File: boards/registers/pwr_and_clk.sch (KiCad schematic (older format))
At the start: 23 parts

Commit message: Fix unconnected nets
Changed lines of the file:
@@
 	1    0    0    -1
 $EndComp
+$Comp
+L power:PWR_FLAG #FLG?
+U 1 1 5EF82079
+P 9650 1200
+F 0 "#FLG?" H 9650 1275 50  0001 C CNN
+F 1 "PWR_FLAG" H 9650 1373 50  0000 C CNN
+F 2 "" H 9650 1200 50  0001 C CNN
+F 3 "~" H 9650 1200 50  0001 C CNN
+	1    9650 1200
+	1    0    0    -1
+$EndComp
+$Comp
+L power:GND #PWR?
+U 1 1 5EF830E9
+P 9650 1200
+F 0 "#PWR?" H 9650 950 50  0001 C CNN
+F 1 "GND" H 9655 1027 50  0000 C CNN
+F 2 "" H 9650 1200 50  0001 C CNN
+F 3 "" H 9650 1200 50  0001 C CNN
+	1    9650 1200
+	1    0    0    -1
+$EndComp
+$Comp
+L power:VCC #PWR?
+U 1 1 5EF8368B
+P 10050 1200
+F 0 "#PWR?" H 10050 1050 50  0001 C CNN
+F 1 "VCC" H 10067 1373 50  0000 C CNN
+F 2 "" H 10050 1200 50  0001 C CNN
+F 3 "" H 10050 1200 50  0001 C CNN
+	1    10050 1200
+	1    0    0    -1
+$EndComp
+$Comp
+L power:PWR_FLAG #FLG?
+U 1 1 5EF840F1
+P 10050 1200
+F 0 "#FLG?" H 10050 1275 50  0001 C CNN
+F 1 "PWR_FLAG" H 10050 1373 50  0000 C CNN
+F 2 "" H 10050 1200 50  0001 C CNN
+F 3 "~" H 10050 1200 50  0001 C CNN
+	1    10050 1200
+	-1   0    0    1
+$EndComp
 $EndSCHEMATC

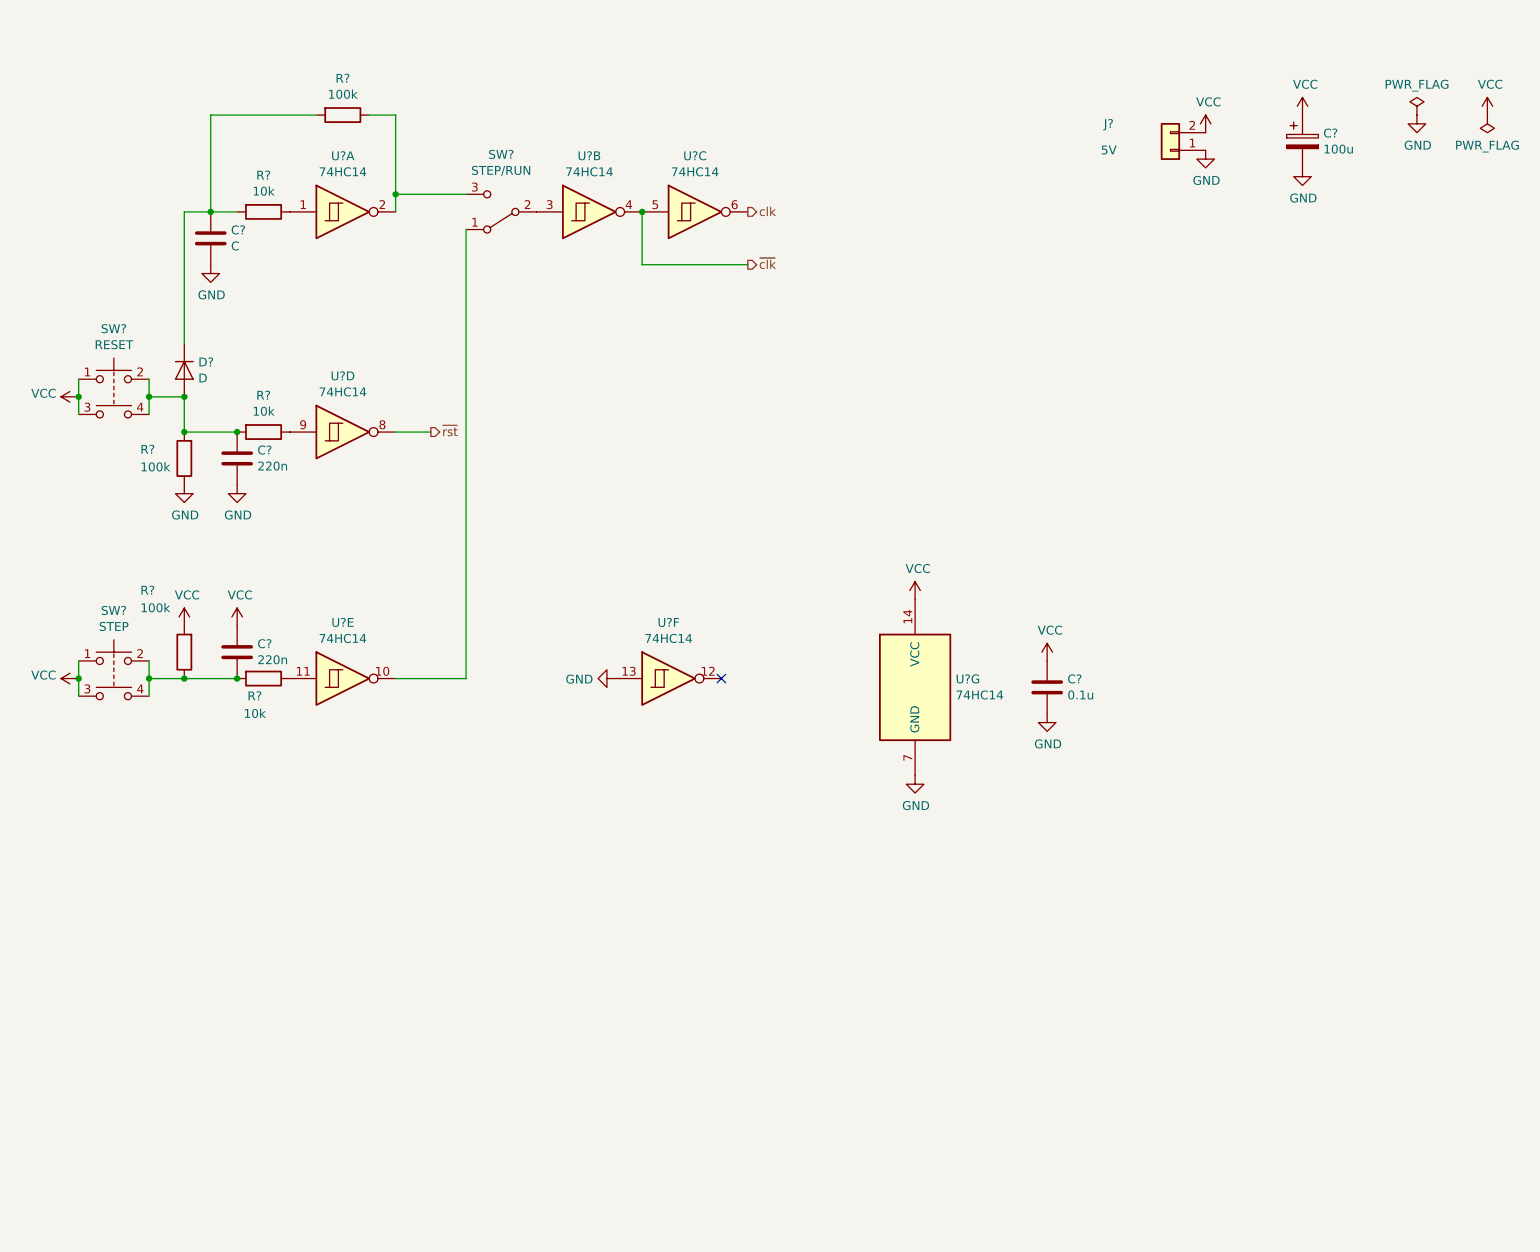
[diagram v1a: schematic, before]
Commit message: Annotated schematics, assigned footprints
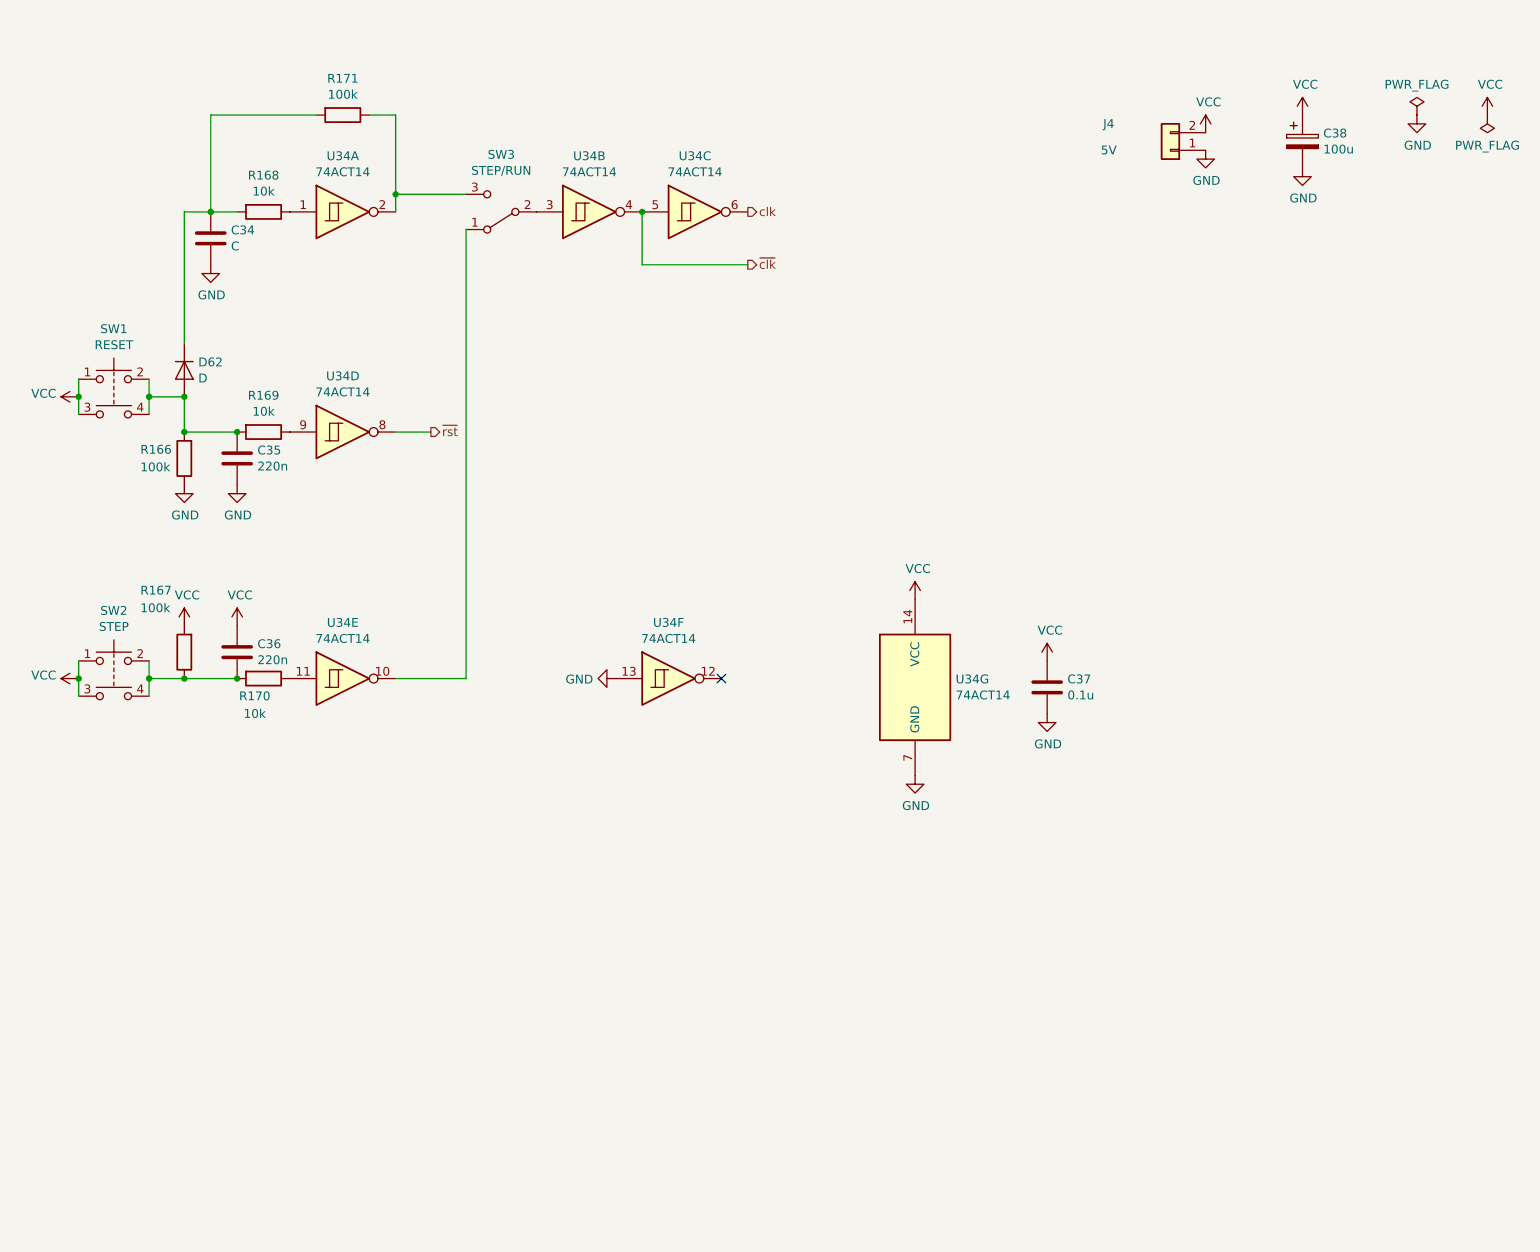
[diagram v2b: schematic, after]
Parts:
- C34, C35, C36: renamed from C?; footprint (none) -> Capacitor_SMD:C_0805_2012Metric
- C37, C38: renamed from C?; footprint (none) -> LED_SMD:LED_0805_2012Metric
- D62: renamed from D?; footprint (none) -> Diode_SMD:D_MiniMELF
- J4: renamed from J?; footprint (none) -> Connector_PinHeader_2.54mm:PinHeader_1x02_P2.54mm_Vertical
- R166, R167, R168, R169, R170, R171: renamed from R?; footprint (none) -> Resistor_SMD:R_0805_2012Metric
- SW1, SW2: renamed from SW?; footprint (none) -> Button_Switch_THT:SW_TH_Tactile_Omron_B3F-10xx
- SW3: renamed from SW?; footprint (none) -> Button_Switch_THT:SW_Slide_1P2T_CK_OS102011MS2Q
- U34: renamed from U?; value 74HC14 -> 74ACT14; footprint (none) -> Package_SO:TSSOP-14_4.4x5mm_P0.65mm

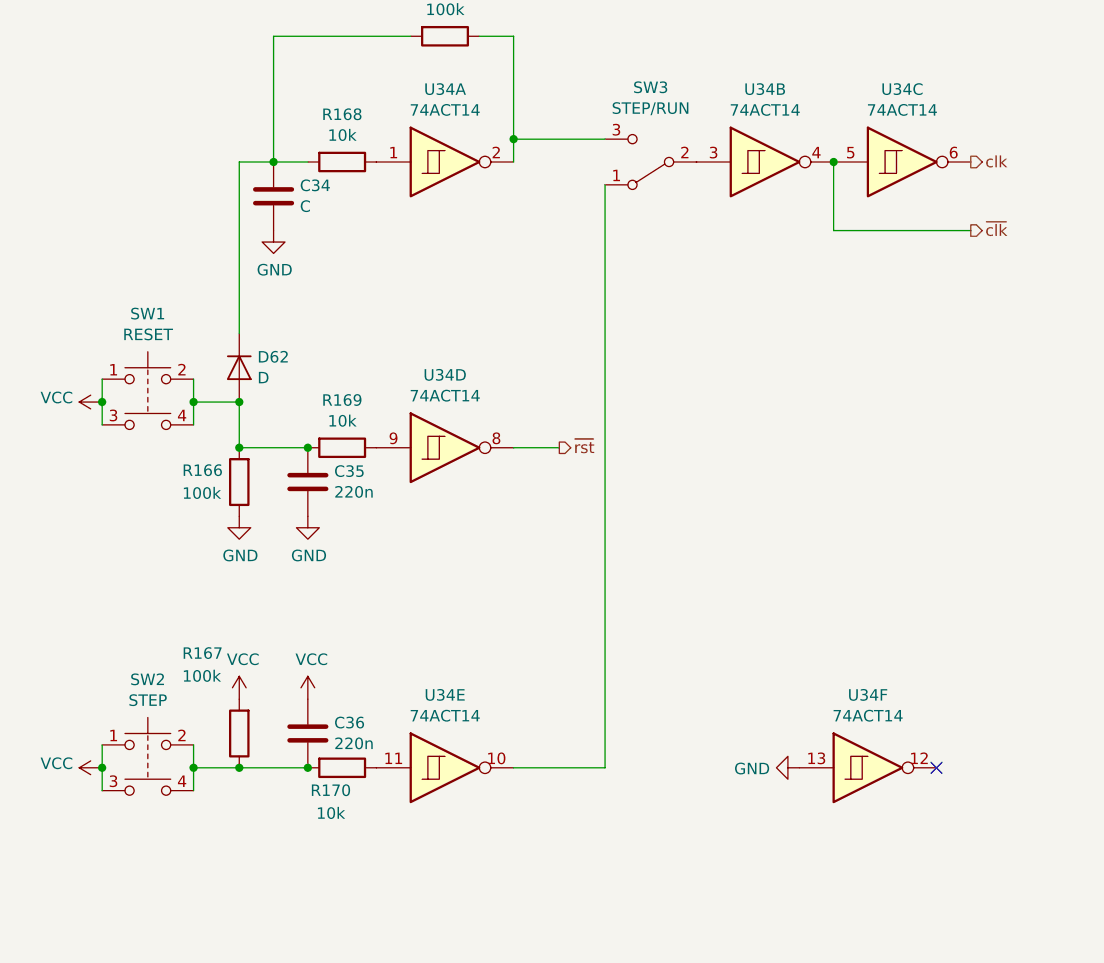
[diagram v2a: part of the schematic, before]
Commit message: CPU registers board
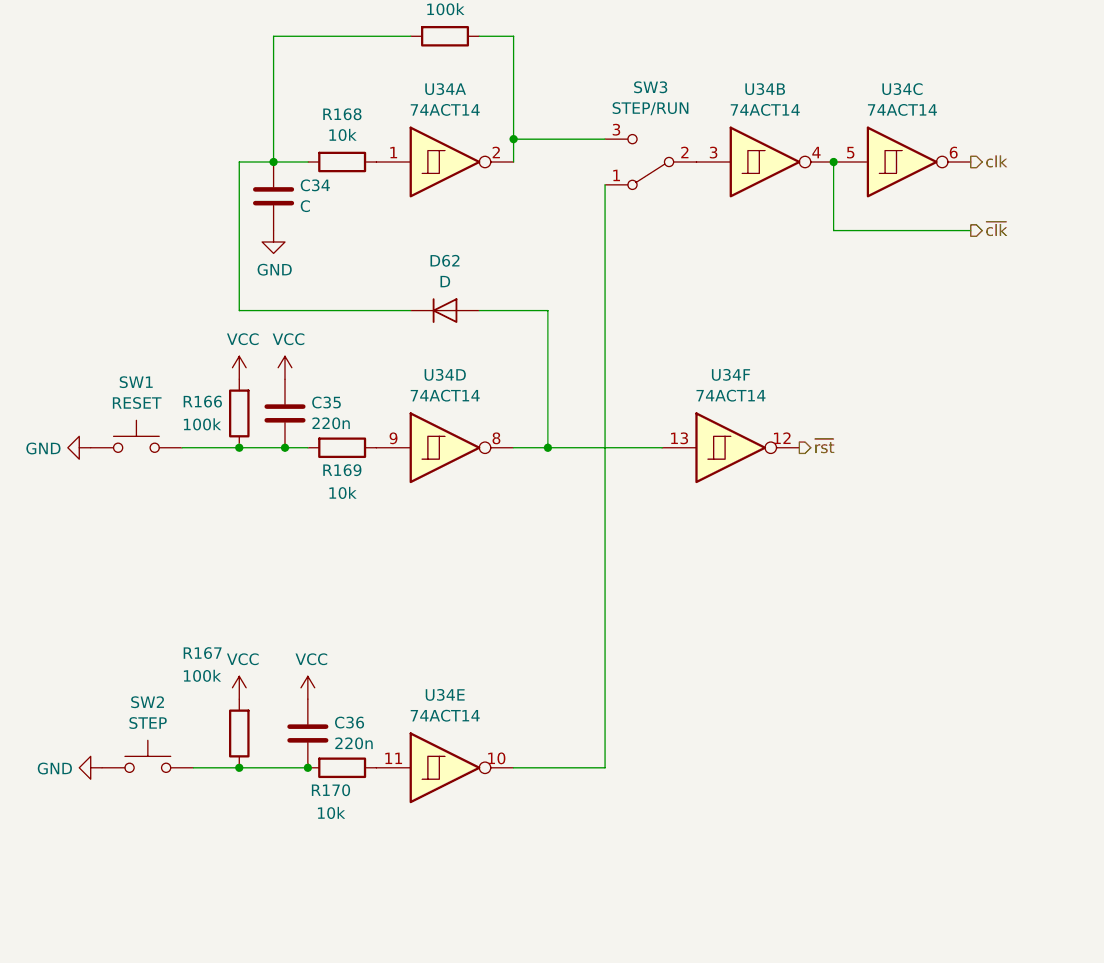
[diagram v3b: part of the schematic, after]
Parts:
- removed SW1: RESET, Button_Switch_THT:SW_TH_Tactile_Omron_B3F-10xx, symbol Switch:SW_Push_Dual
- removed SW2: STEP, Button_Switch_THT:SW_TH_Tactile_Omron_B3F-10xx, symbol Switch:SW_Push_Dual
- added SW1: RESET, Button_Switch_THT:SW_PUSH_6mm, symbol Switch:SW_Push
- added SW2: STEP, Button_Switch_THT:SW_PUSH_6mm, symbol Switch:SW_Push
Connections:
- net GND: now also SW1.1, SW2.1; no longer C35.2, R166.1, U34.13
- net VCC: now also C35.1, R166.2
- net ~rst: now also U34.12; no longer U34.8
- net at C36.2, R167.1, R170.2: now also SW2.2
- new net: C35.2, R166.1, R169.2, SW1.2
- new net: D62.2 (A), U34.13, U34.8
- no-connect marks 1 -> 0
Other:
- moved on the sheet: C35, D62, R166, U34F
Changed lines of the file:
@@
 Text HLabel 5850 1750 2    50   Output ~ 0
 clk
-Text HLabel 4050 3000 2    50   Output ~ 0
+Text HLabel 5100 3000 2    50   Output ~ 0
 ~rst
 Text HLabel 5850 2050 2    50   Output ~ 0
@@
 L Device:R R166
 U 1 1 5EF0FCD1
-P 2650 3150
-F 0 "R166" H 2900 3100 50  0000 R CNN
-F 1 "100k" H 2900 3200 50  0000 R CNN
-F 2 "Resistor_SMD:R_0805_2012Metric" V 2580 3150 50  0001 C CNN
-F 3 "~" H 2650 3150 50  0001 C CNN
-	1    2650 3150
+P 2650 2850
+F 0 "R166" H 2900 2800 50  0000 R CNN
+F 1 "100k" H 2900 2900 50  0000 R CNN
+F 2 "Resistor_SMD:R_0805_2012Metric" V 2580 2850 50  0001 C CNN
+F 3 "~" H 2650 2850 50  0001 C CNN
+	1    2650 2850
 	-1   0    0    1
-$EndComp
-$Comp
-L power:GND #PWR0219
-U 1 1 5EF10373
-P 2650 3300
-F 0 "#PWR0219" H 2650 3050 50  0001 C CNN
-F 1 "GND" H 2655 3127 50  0000 C CNN
-F 2 "" H 2650 3300 50  0001 C CNN
-F 3 "" H 2650 3300 50  0001 C CNN
-	1    2650 3300
-	1    0    0    -1
 $EndComp
 $Comp
@@
 U 1 1 5EF12F5C
 P 3100 3000
-F 0 "R169" V 2893 3000 50  0000 C CNN
-F 1 "10k" V 2984 3000 50  0000 C CNN
+F 0 "R169" V 3200 3000 50  0000 C CNN
+F 1 "10k" V 3300 3000 50  0000 C CNN
 F 2 "Resistor_SMD:R_0805_2012Metric" V 3030 3000 50  0001 C CNN
 F 3 "~" H 3100 3000 50  0001 C CNN
@@
 L Device:C C35
 U 1 1 5EF136E4
-P 2950 3150
-F 0 "C35" H 3065 3196 50  0000 L CNN
-F 1 "220n" H 3065 3105 50  0000 L CNN
-F 2 "Capacitor_SMD:C_0805_2012Metric" H 2988 3000 50  0001 C CNN
-F 3 "~" H 2950 3150 50  0001 C CNN
-	1    2950 3150
-	1    0    0    -1
-$EndComp
-$Comp
-L power:GND #PWR0222
-U 1 1 5EF14A7A
-P 2950 3300
-F 0 "#PWR0222" H 2950 3050 50  0001 C CNN
-F 1 "GND" H 2955 3127 50  0000 C CNN
-F 2 "" H 2950 3300 50  0001 C CNN
-F 3 "" H 2950 3300 50  0001 C CNN
-	1    2950 3300
-	1    0    0    -1
-$EndComp
-Wire Wire Line
-	2650 3000 2950 3000
-Connection ~ 2950 3000
-$Comp
-L Switch:SW_Push_Dual SW1
-U 1 1 5EF16B54
-P 2250 2700
-F 0 "SW1" H 2250 2985 50  0000 C CNN
-F 1 "RESET" H 2250 2894 50  0000 C CNN
-F 2 "Button_Switch_THT:SW_TH_Tactile_Omron_B3F-10xx" H 2250 2900 50  0001 C CNN
-F 3 "~" H 2250 2900 50  0001 C CNN
-	1    2250 2700
-	1    0    0    -1
-$EndComp
-Wire Wire Line
-	2450 2700 2450 2800
-Wire Wire Line
-	2650 3000 2650 2800
-Wire Wire Line
-	2650 2800 2450 2800
-Connection ~ 2650 3000
-Connection ~ 2450 2800
-Wire Wire Line
-	2450 2800 2450 2900
-Wire Wire Line
-	2050 2700 2050 2800
-$Comp
-L power:VCC #PWR0217
-U 1 1 5EF17FE7
-P 2050 2800
-F 0 "#PWR0217" H 2050 2650 50  0001 C CNN
-F 1 "VCC" V 2068 2927 50  0000 L CNN
-F 2 "" H 2050 2800 50  0001 C CNN
-F 3 "" H 2050 2800 50  0001 C CNN
-	1    2050 2800
-	0    -1   -1   0
-$EndComp
-Connection ~ 2050 2800
-Wire Wire Line
-	2050 2800 2050 2900
+P 2850 2850
+F 0 "C35" H 2965 2896 50  0000 L CNN
+F 1 "220n" H 2965 2805 50  0000 L CNN
+F 2 "Capacitor_SMD:C_0805_2012Metric" H 2888 2700 50  0001 C CNN
+F 3 "~" H 2850 2850 50  0001 C CNN
+	1    2850 2850
+	1    0    0    -1
+$EndComp
+Wire Wire Line
+	2650 3000 2850 3000
 $Comp
 L Device:D D62
 U 1 1 5EF19BA6
-P 2650 2650
-F 0 "D62" V 2604 2729 50  0000 L CNN
-F 1 "D" V 2695 2729 50  0000 L CNN
-F 2 "Diode_SMD:D_MiniMELF" H 2650 2650 50  0001 C CNN
-F 3 "~" H 2650 2650 50  0001 C CNN
-	1    2650 2650
-	0    1    1    0
-$EndComp
-Connection ~ 2650 2800
-Wire Wire Line
-	2650 2500 2650 1750
+P 3550 2400
+F 0 "D62" H 3550 2616 50  0000 C CNN
+F 1 "D" H 3550 2525 50  0000 C CNN
+F 2 "Diode_SMD:D_MiniMELF" H 3550 2400 50  0001 C CNN
+F 3 "~" H 3550 2400 50  0001 C CNN
+	1    3550 2400
+	1    0    0    -1
+$EndComp
 Wire Wire Line
 	2650 1750 2800 1750
-Wire Wire Line
-	4050 3000 3850 3000
 $Comp
 L 74xx:74HC14 U34
@@
 	5250 2050 5250 1750
 Connection ~ 5250 1750
-$Comp
-L Switch:SW_Push_Dual SW2
-U 1 1 5EF2196E
-P 2250 4300
-F 0 "SW2" H 2250 4585 50  0000 C CNN
-F 1 "STEP" H 2250 4494 50  0000 C CNN
-F 2 "Button_Switch_THT:SW_TH_Tactile_Omron_B3F-10xx" H 2250 4500 50  0001 C CNN
-F 3 "~" H 2250 4500 50  0001 C CNN
-	1    2250 4300
-	1    0    0    -1
-$EndComp
-Wire Wire Line
-	2050 4300 2050 4400
-$Comp
-L power:VCC #PWR0218
-U 1 1 5EF2A747
-P 2050 4400
-F 0 "#PWR0218" H 2050 4250 50  0001 C CNN
-F 1 "VCC" V 2068 4527 50  0000 L CNN
-F 2 "" H 2050 4400 50  0001 C CNN
-F 3 "" H 2050 4400 50  0001 C CNN
-	1    2050 4400
-	0    -1   -1   0
-$EndComp
-Connection ~ 2050 4400
-Wire Wire Line
-	2050 4400 2050 4500
-Wire Wire Line
-	2450 4500 2450 4400
 $Comp
 L 74xx:74HC14 U34
@@
 	2650 4400 2450 4400
 Connection ~ 2650 4400
-Connection ~ 2450 4400
-Wire Wire Line
-	2450 4400 2450 4300
 $Comp
 L Switch:SW_SPDT SW3
@@
 L 74xx:74HC14 U34
 U 6 1 5EF430CB
-P 5400 4400
-F 0 "U34" H 5400 4717 50  0000 C CNN
-F 1 "74ACT14" H 5400 4626 50  0000 C CNN
-F 2 "Package_SO:TSSOP-14_4.4x5mm_P0.65mm" H 5400 4400 50  0001 C CNN
-F 3 "http://www.ti.com/lit/gpn/sn74HC14" H 5400 4400 50  0001 C CNN
-	6    5400 4400
-	1    0    0    -1
-$EndComp
-$Comp
-L power:GND #PWR0224
-U 1 1 5EF45DA1
-P 5100 4400
-F 0 "#PWR0224" H 5100 4150 50  0001 C CNN
-F 1 "GND" V 5105 4272 50  0000 R CNN
-F 2 "" H 5100 4400 50  0001 C CNN
-F 3 "" H 5100 4400 50  0001 C CNN
-	1    5100 4400
-	0    1    1    0
-$EndComp
-NoConn ~ 5700 4400
+P 4800 3000
+F 0 "U34" H 4800 3317 50  0000 C CNN
+F 1 "74ACT14" H 4800 3226 50  0000 C CNN
+F 2 "Package_SO:TSSOP-14_4.4x5mm_P0.65mm" H 4800 3000 50  0001 C CNN
+F 3 "http://www.ti.com/lit/gpn/sn74HC14" H 4800 3000 50  0001 C CNN
+	6    4800 3000
+	1    0    0    -1
+$EndComp
 $Comp
 L 74xx:74HC14 U34
@@
 	-1   0    0    1
 $EndComp
+$Comp
+L Switch:SW_Push SW2
+U 1 1 5FB8F28D
+P 2250 4400
+F 0 "SW2" H 2250 4685 50  0000 C CNN
+F 1 "STEP" H 2250 4594 50  0000 C CNN
+F 2 "Button_Switch_THT:SW_PUSH_6mm" H 2250 4600 50  0001 C CNN
+F 3 "~" H 2250 4600 50  0001 C CNN
+	1    2250 4400
+	1    0    0    -1
+$EndComp
+$Comp
+L Switch:SW_Push SW1
+U 1 1 5FB8F94E
+P 2200 3000
+F 0 "SW1" H 2200 3285 50  0000 C CNN
+F 1 "RESET" H 2200 3194 50  0000 C CNN
+F 2 "Button_Switch_THT:SW_PUSH_6mm" H 2200 3200 50  0001 C CNN
+F 3 "~" H 2200 3200 50  0001 C CNN
+	1    2200 3000
+	1    0    0    -1
+$EndComp
+Wire Wire Line
+	4500 3000 4000 3000
+Wire Wire Line
+	4000 3000 4000 2400
+Wire Wire Line
+	4000 2400 3700 2400
+Connection ~ 4000 3000
+Wire Wire Line
+	4000 3000 3850 3000
+Wire Wire Line
+	3400 2400 2650 2400
+Wire Wire Line
+	2650 2400 2650 1750
+$Comp
+L power:GND #PWR?
+U 1 1 5FBA3876
+P 2000 3000
+F 0 "#PWR?" H 2000 2750 50  0001 C CNN
+F 1 "GND" V 2005 2872 50  0000 R CNN
+F 2 "" H 2000 3000 50  0001 C CNN
+F 3 "" H 2000 3000 50  0001 C CNN
+	1    2000 3000
+	0    1    1    0
+$EndComp
+$Comp
+L power:GND #PWR?
+U 1 1 5FBA3DBF
+P 2050 4400
+F 0 "#PWR?" H 2050 4150 50  0001 C CNN
+F 1 "GND" V 2055 4272 50  0000 R CNN
+F 2 "" H 2050 4400 50  0001 C CNN
+F 3 "" H 2050 4400 50  0001 C CNN
+	1    2050 4400
+	0    1    1    0
+$EndComp
+Wire Wire Line
+	2950 3000 2850 3000
+Connection ~ 2850 3000
+$Comp
+L power:VCC #PWR?
+U 1 1 5FBA8516
+P 2650 2700
+F 0 "#PWR?" H 2650 2550 50  0001 C CNN
+F 1 "VCC" H 2667 2873 50  0000 C CNN
+F 2 "" H 2650 2700 50  0001 C CNN
+F 3 "" H 2650 2700 50  0001 C CNN
+	1    2650 2700
+	1    0    0    -1
+$EndComp
+$Comp
+L power:VCC #PWR?
+U 1 1 5FBA8A47
+P 2850 2700
+F 0 "#PWR?" H 2850 2550 50  0001 C CNN
+F 1 "VCC" H 2867 2873 50  0000 C CNN
+F 2 "" H 2850 2700 50  0001 C CNN
+F 3 "" H 2850 2700 50  0001 C CNN
+	1    2850 2700
+	1    0    0    -1
+$EndComp
+Wire Wire Line
+	2400 3000 2650 3000
+Connection ~ 2650 3000
 $EndSCHEMATC
